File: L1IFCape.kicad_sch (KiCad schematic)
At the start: 85 parts, among them J1 RF_Shield_One_Piece, J2 SMA, J3 MMCX, P8 BeagleBone_Black_Header, P9 BeagleBone_Black_Header, U1 24CS256, U2 MAX2769BETI+T, U3 MAX31343ETAY+T, U4 TPS717285DCK, U5 TPS717285DCK, X1 SIT5156, X2 QPQ1060

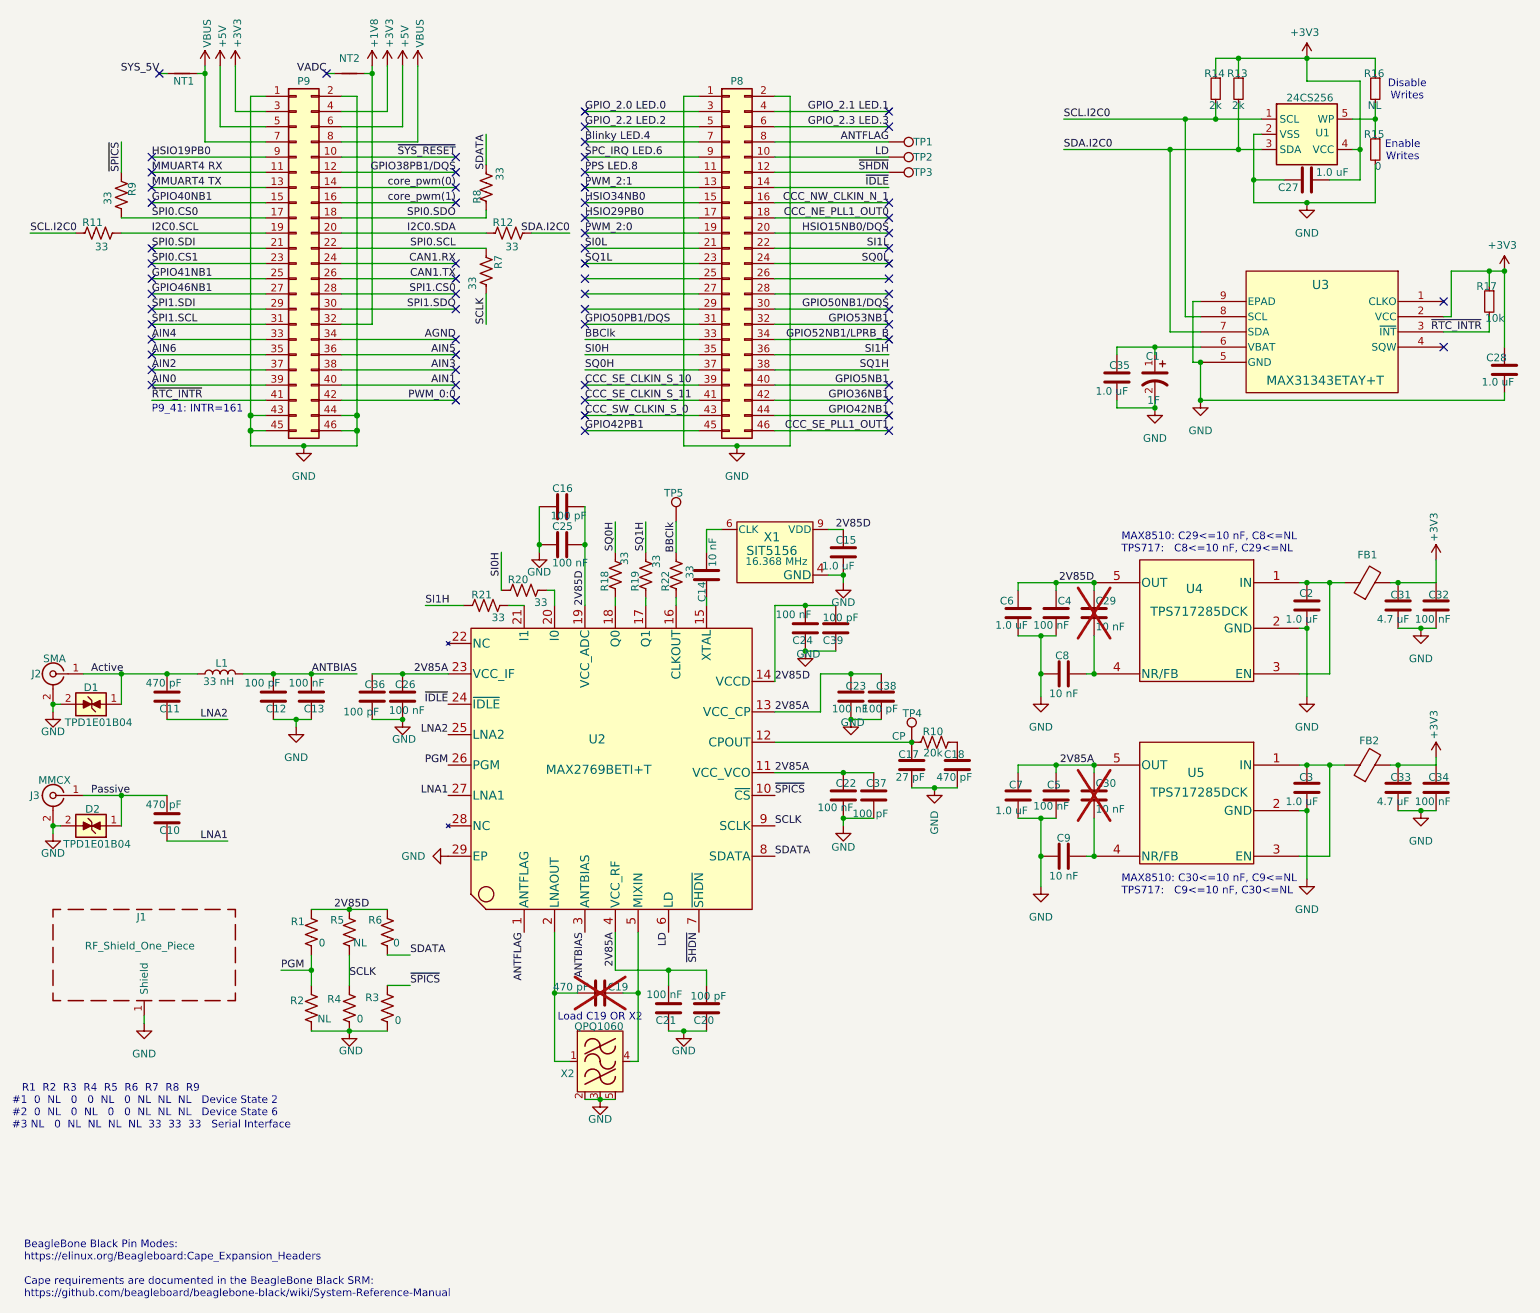
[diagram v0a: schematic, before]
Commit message: Added schematic to the back and cleaned up some schematic issues
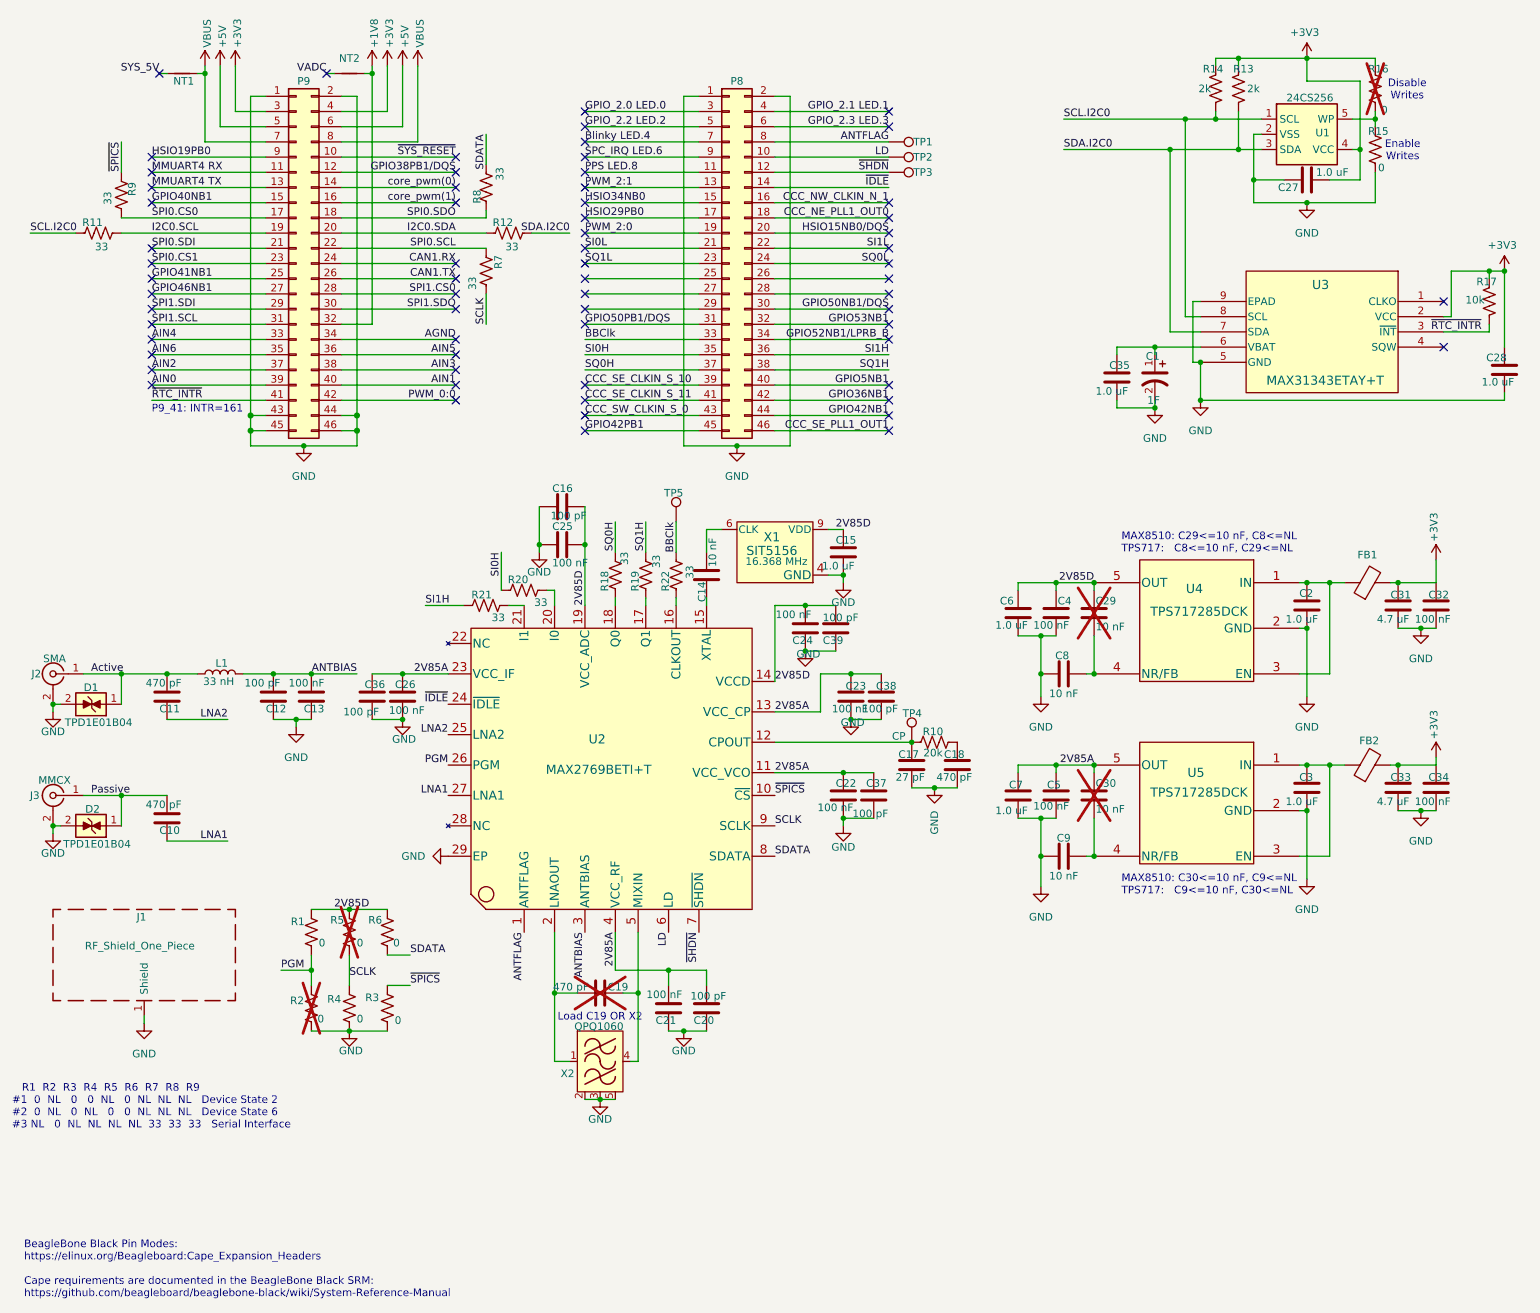
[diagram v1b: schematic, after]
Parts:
- removed R15: 0, L1IF:R_0603_1608Metric, symbol L1IF:R_Small
- removed R16: NL, L1IF:R_0603_1608Metric, symbol L1IF:R_Small
- added R15, R16: 0, L1IF:R_0603_1608Metric, symbol L1IF:Resistor
- R13, R14: symbol L1IF:R_Small -> L1IF:Resistor
- R17: symbol L1IF:10k_0603 -> L1IF:Resistor
- R2, R5: value NL -> 0; now not fitted
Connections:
- net +3V3: now also R16.2
- net GND: now also R15.1
- net at U1.5 (WP): now also R15.2, R16.1

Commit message: Cleaned up BOM
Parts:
- C10, C11, C15, C18, C2, C27, C28, C3, C35, C6, C7, FB1, FB2: MFR (none) -> Murata
- C12, C20: MFR (none) -> Murata; VPN (none) -> 490-GCM1885C2A101FA16DCT-ND
- C13, C14, C17, C21, C22, C23, C24, C25, C26, C31, C32, C33, C34, C4, C5, C8, C9: MFR (none) -> Kemet
- C16, C36, C37, C38, C39: MFR (none) -> Murata; MPN C0603C104K5RACAUTO -> GCM1885C2A101FA16D; VPN (none) -> 490-GCM1885C2A101FA16DCT-ND
- C19: MFR (none) -> Murata; VPN (none) -> 490-GCM1885C2A471FA16DCT-ND
- C29, C30: MFR (none) -> Kemet; MPN (none) -> C0603C103F3GECAUTO; VPN (none) -> 399-C0603C103F3GECAUTOCT-ND; Vendor (none) -> DigiKey
- J1: MFR (none) -> Laird

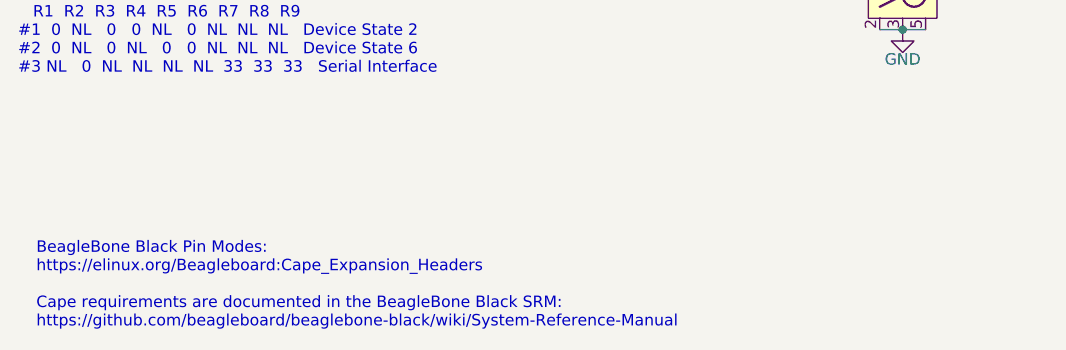
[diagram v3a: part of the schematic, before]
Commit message: Updated CERN License Wording
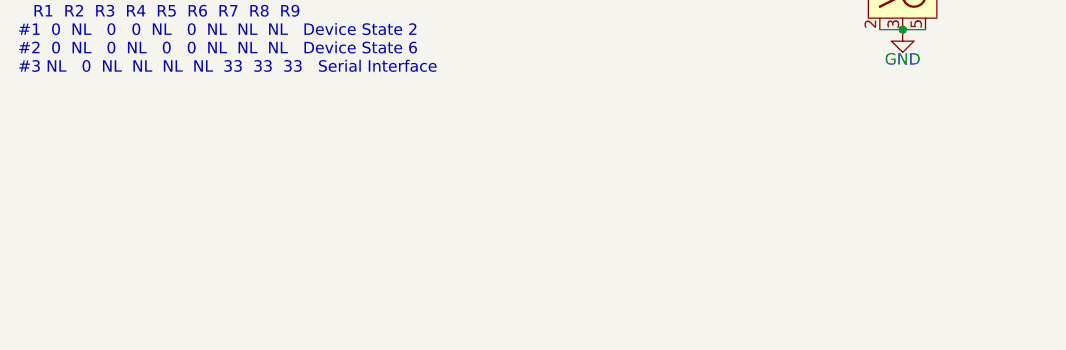
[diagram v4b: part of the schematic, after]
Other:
- note removed: "BeagleBone Black Pin Modes: https://elinux.org/Beagleboard:Cape_Expansion_Headers Cape requirements are documented in the BeagleBone Black SRM: https://github.com/beagleboard/beaglebone-black/wiki/System-Reference-Manual"
- company: (none) -> NavStarGPS.US
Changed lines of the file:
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@@
 		(date "2026-08-15")
 		(rev "${SCH_VER}")
-		(comment 1 "https://cern.ch/cern-ohl ")
-		(comment 2 "License: CERN-OHL-S-2.0")
+		(company "NavStarGPS.US")
+		(comment 1 "SPDX-License-Identifier: CERN-OHL-S-2.0")
+		(comment 2 "Licensed under the CERN Open Hardware Licence Version 2 - Strongly Reciprocal")
 		(comment 3 "Maxim 2769 BeagleV-Fire Cape")
 		(comment 4 "Author: W. Kyle Gilbertson")
-	)
-	(text "BeagleBone Black Pin Modes:\nhttps://elinux.org/Beagleboard:Cape_Expansion_Headers\n\nCape requirements are documented in the BeagleBone Black SRM:\nhttps://github.com/beagleboard/beaglebone-black/wiki/System-Reference-Manual"
-		(exclude_from_sim no)
-		(at 16.764 230.124 0)
-		(effects
-			(font
-				(size 1.27 1.27)
-			)
-			(justify left bottom)
-		)
+		(comment 5 "https://cern.ch/cern-ohl ")
 	)
 	(text "   R1  R2  R3  R4  R5  R6  R7  R8  R9\n#1  0  NL   0   0  NL   0  NL  NL  NL   Device State 2\n#2  0  NL   0  NL   0   0  NL  NL  NL   Device State 6\n#3 NL   0  NL  NL  NL  NL  33  33  33   Serial Interface"

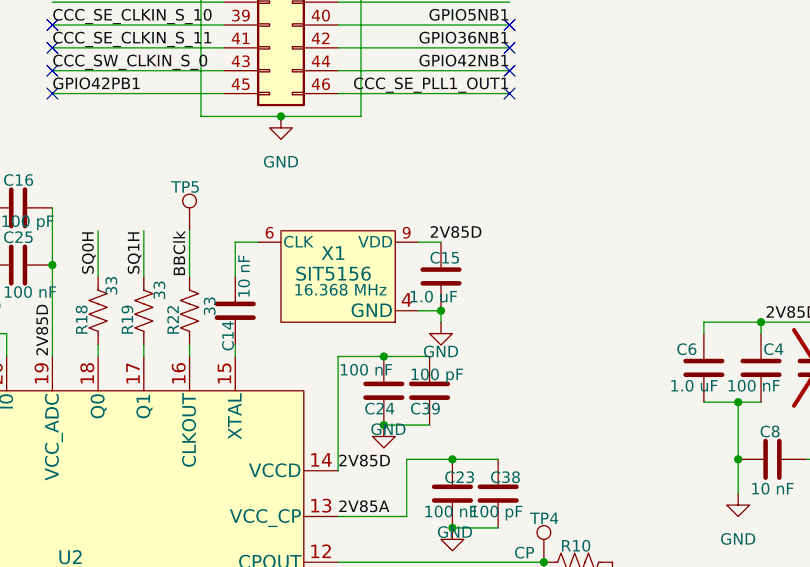
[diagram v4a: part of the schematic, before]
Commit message: Added I2C connection to SiT5156
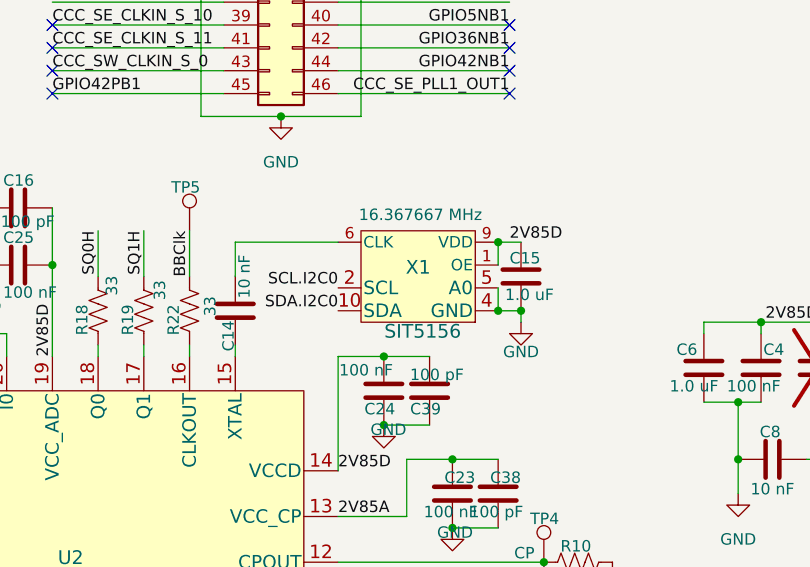
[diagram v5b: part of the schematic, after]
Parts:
- X1: Availability (none) -> https://www.sitime.com/products/ultrastable-mhz-super-tcxos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; MPN SIT5156AICFK-30N0-16.368000 -> SiT5156AICFK028IT-16.367667; Notes 16.368 MHz -> 16.367667 MHz; VPN 1473-SIT5156AICFK-30N0-16.368000-ND -> (none); Vendor DigiKey -> SiTime; Vendor PN 1473-SIT5156AICFK-30N0-16.368000-ND -> SiT5156AICFK028IT-16.367667
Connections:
- net 2V85D: now also X1.1 (OE)
- net GND: now also X1.5 (A0)
- net SCL.I2C0: now also X1.2 (SCL)
- net SDA.I2C0: now also X1.10 (SDA)
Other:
- moved on the sheet: C15

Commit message: SiT5156 Part Number...TBC
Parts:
- X1: symbol L1IF:SIT5156AICFA-30N0-16.368000_1 -> L1IF:SiT5156AICFK028IT-16.367667; Vendor SiTime -> DigiKey
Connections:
- net 2V85D: now also X1.8 (OE); no longer X1.1 (OE)
- net GND: now also X1.3 (A0); no longer X1.5 (A0)
- net SDA.I2C0: now also X1.1 (SDA); no longer X1.10 (SDA)
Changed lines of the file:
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@@
 	)
 	(symbol
-		(lib_id "L1IF:SIT5156AICFA-30N0-16.368000_1")
+		(lib_id "L1IF:SiT5156AICFK028IT-16.367667")
 		(at 160.02 109.22 180)
 		(unit 1)
@@
 			)
 		)
-		(property "Description" "MEMS OSC DCTCXO 16.367667 MHZ DC"
+		(property "Description" "MEMS OSC TCXO 16.367667 MHZ"
 			(at 162.814 113.792 0)
 			(hide yes)
@@
 			)
 		)
-		(property "Vendor" "SiTime"
+		(property "Vendor" "DigiKey"
 			(at 151.13 129.54 0)
 			(hide yes)

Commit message: Ordered Boards From OshPark for Rev D4
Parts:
- X1: value SIT5156 -> SIT5155; symbol L1IF:SiT5156AICFK028IT-16.367667 -> L1IF:SiT5155AICFKG28IT-16.367667; Alternate1 (none) -> SiT5356AICFQG28IT-16.367667; Alternate2 (none) -> SiT5358AICFSG28IT-16.367667; MPN SiT5156AICFK028IT-16.367667 -> SiT5155AICFKG28IT-16.367667; Vendor DigiKey -> SiTime; Vendor PN SiT5156AICFK028IT-16.367667 -> SiT5155AICFKG28IT-16.367667
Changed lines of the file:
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@@
 	)
 	(symbol
-		(lib_id "L1IF:SiT5156AICFK028IT-16.367667")
+		(lib_id "L1IF:SiT5155AICFKG28IT-16.367667")
 		(at 160.02 109.22 180)
 		(unit 1)
@@
 			)
 		)
-		(property "Value" "SIT5156"
+		(property "Value" "SIT5155"
 			(at 151.638 111.506 0)
 			(show_name no)
@@
 			)
 		)
-		(property "Datasheet" "https://www.sitime.com/support/resource-library/datasheets/sit5156-datasheet"
+		(property "Datasheet" "https://www.sitime.com/support/resource-library/datasheets/sit5155-datasheet"
 			(at 156.21 125.73 0)
 			(hide yes)
@@
 			)
 		)
-		(property "Description" "MEMS OSC TCXO 16.367667 MHZ"
+		(property "Description" "MEMS OSC DCTCXO 16.367667 MHZ"
 			(at 162.814 113.792 0)
 			(hide yes)
@@
 			)
 		)
-		(property "MPN" "SiT5156AICFK028IT-16.367667"
+		(property "MPN" "SiT5155AICFKG28IT-16.367667"
 			(at 151.13 121.92 0)
 			(hide yes)
@@
 			)
 		)
-		(property "Vendor" "DigiKey"
+		(property "Vendor" "SiTime"
 			(at 151.13 129.54 0)
 			(hide yes)
@@
 			)
 		)
-		(property "Vendor PN" "SiT5156AICFK028IT-16.367667"
+		(property "Vendor PN" "SiT5155AICFKG28IT-16.367667"
 			(at 151.13 123.19 0)
 			(hide yes)
@@
 			(at 160.02 109.22 0)
 			(hide yes)
+			(show_name no)
+			(do_not_autoplace no)
+			(effects
+				(font
+					(size 1.27 1.27)
+				)
+			)
+		)
+		(property "Alternate1" "SiT5356AICFQG28IT-16.367667"
+			(at 160.02 109.22 0)
+			(hide yes)
+			(show_name no)
+			(do_not_autoplace no)
+			(effects
+				(font
+					(size 1.27 1.27)
+				)
+			)
+		)
+		(property "Alternate2" "SiT5358AICFSG28IT-16.367667"
+			(at 160.02 109.22 0)
+			(hide yes)
